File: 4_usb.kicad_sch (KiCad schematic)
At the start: 4 parts, among them J401 USB_C_Receptacle_USB2.0, U401 USBLC6-2SC6

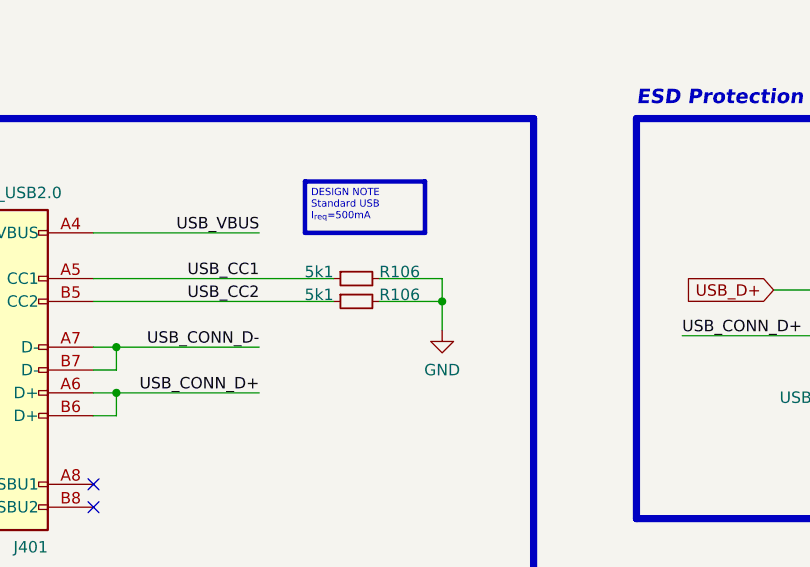
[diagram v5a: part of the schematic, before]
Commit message: feat: finished inverter placement and routing
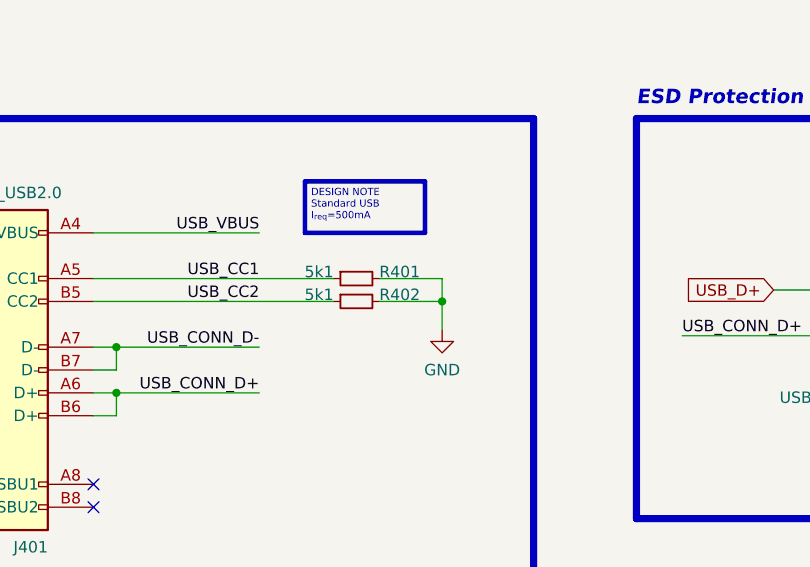
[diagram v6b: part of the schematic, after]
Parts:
- renumbered R106 to R401, R106 to R402
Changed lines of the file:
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@@
   (symbol (lib_id "Device:R_Small") (at 134.62 85.09 90) (mirror x) (unit 1)
     (in_bom yes) (on_board yes) (dnp no)
-    (property "Reference" "R106" (at 137.16 85.09 90)
+    (property "Reference" "R401" (at 137.16 85.09 90)
       (effects (font (size 1.27 1.27)) (justify right bottom))
     )
@@
     (instances
       (project "ESC_R1"
-        (path "/9dea2e18-5867-4ed4-a12d-7ee109225de0/bab0431c-ca33-4c57-9dbe-00ccaf05ca0f"
-          (reference "R106") (unit 1)
-        )
         (path "/9dea2e18-5867-4ed4-a12d-7ee109225de0/4b568fb1-3ffb-4d91-93b3-473275569108"
           (reference "R401") (unit 1)
@@
   (symbol (lib_id "power:GND") (at 144.145 90.805 0) (mirror y) (unit 1)
     (in_bom yes) (on_board yes) (dnp no)
-    (property "Reference" "#PWR03" (at 144.145 97.155 0)
+    (property "Reference" "#PWR011" (at 144.145 97.155 0)
       (effects (font (size 1.27 1.27)) hide)
     )
@@
     (instances
       (project "ESC_R1"
-        (path "/9dea2e18-5867-4ed4-a12d-7ee109225de0/52041989-aba3-4113-ba04-ece39669328f"
-          (reference "#PWR03") (unit 1)
-        )
         (path "/9dea2e18-5867-4ed4-a12d-7ee109225de0/4b568fb1-3ffb-4d91-93b3-473275569108"
           (reference "#PWR011") (unit 1)
@@
   (symbol (lib_id "power:GND") (at 196.215 102.87 0) (unit 1)
     (in_bom yes) (on_board yes) (dnp no)
-    (property "Reference" "#PWR03" (at 196.215 109.22 0)
+    (property "Reference" "#PWR08" (at 196.215 109.22 0)
       (effects (font (size 1.27 1.27)) hide)
     )
@@
     (instances
       (project "ESC_R1"
-        (path "/9dea2e18-5867-4ed4-a12d-7ee109225de0/52041989-aba3-4113-ba04-ece39669328f"
-          (reference "#PWR03") (unit 1)
-        )
         (path "/9dea2e18-5867-4ed4-a12d-7ee109225de0/4b568fb1-3ffb-4d91-93b3-473275569108"
           (reference "#PWR08") (unit 1)
@@
   (symbol (lib_id "power:GND") (at 90.17 123.825 0) (mirror y) (unit 1)
     (in_bom yes) (on_board yes) (dnp no)
-    (property "Reference" "#PWR03" (at 90.17 130.175 0)
+    (property "Reference" "#PWR0501" (at 90.17 130.175 0)
       (effects (font (size 1.27 1.27)) hide)
     )
@@
     (instances
       (project "ESC_R1"
-        (path "/9dea2e18-5867-4ed4-a12d-7ee109225de0/52041989-aba3-4113-ba04-ece39669328f"
-          (reference "#PWR03") (unit 1)
-        )
         (path "/9dea2e18-5867-4ed4-a12d-7ee109225de0/4b568fb1-3ffb-4d91-93b3-473275569108"
           (reference "#PWR0501") (unit 1)
@@
   (symbol (lib_id "Device:R_Small") (at 134.62 87.63 90) (mirror x) (unit 1)
     (in_bom yes) (on_board yes) (dnp no)
-    (property "Reference" "R106" (at 137.16 87.63 90)
+    (property "Reference" "R402" (at 137.16 87.63 90)
       (effects (font (size 1.27 1.27)) (justify right bottom))
     )
@@
     (instances
       (project "ESC_R1"
-        (path "/9dea2e18-5867-4ed4-a12d-7ee109225de0/bab0431c-ca33-4c57-9dbe-00ccaf05ca0f"
-          (reference "R106") (unit 1)
-        )
         (path "/9dea2e18-5867-4ed4-a12d-7ee109225de0/4b568fb1-3ffb-4d91-93b3-473275569108"
           (reference "R402") (unit 1)
